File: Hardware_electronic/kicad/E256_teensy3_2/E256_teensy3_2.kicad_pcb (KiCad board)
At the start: 2 copper layers, 2 parts, among them U1 e256_pad_16x16, U2 Teensy3.2

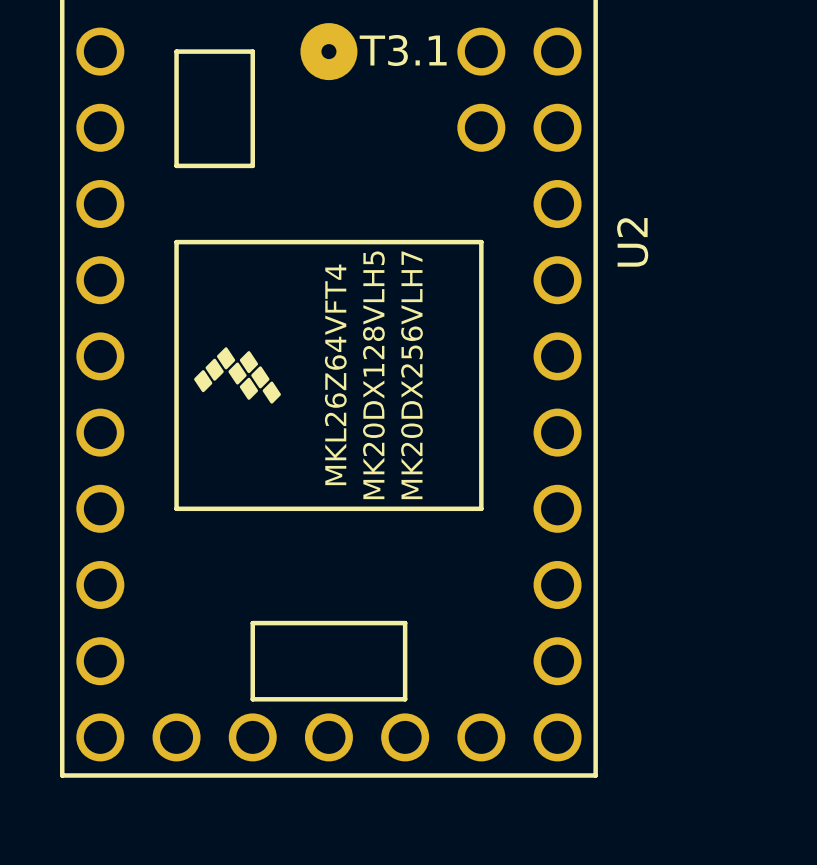
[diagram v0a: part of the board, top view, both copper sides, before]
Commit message: Adde pins under PCB to the Teensy lib
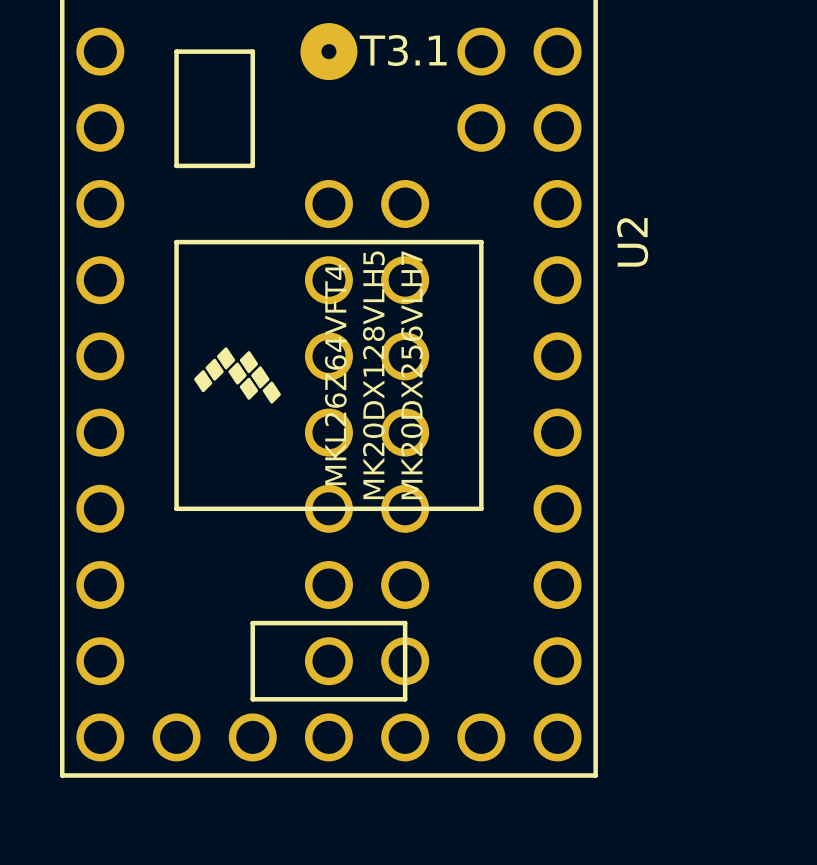
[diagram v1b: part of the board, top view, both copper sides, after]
